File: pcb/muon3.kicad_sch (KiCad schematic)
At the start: 0 parts

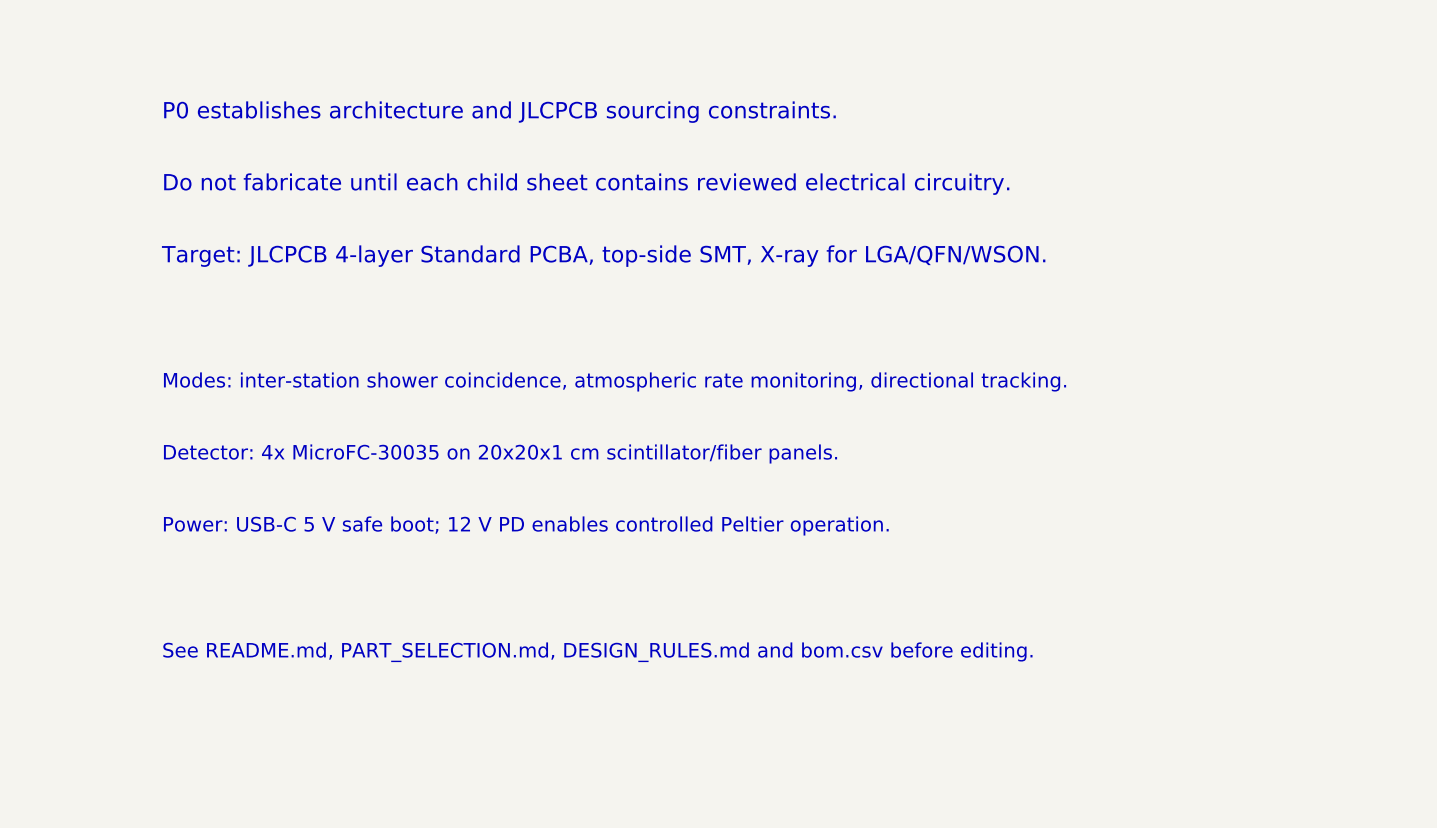
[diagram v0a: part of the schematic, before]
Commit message: Update paper with latest architecture, add openEMS EM simulations (RF, SI, PDN), update schematics with real symbols/wires, add 3D models and openEMS figures
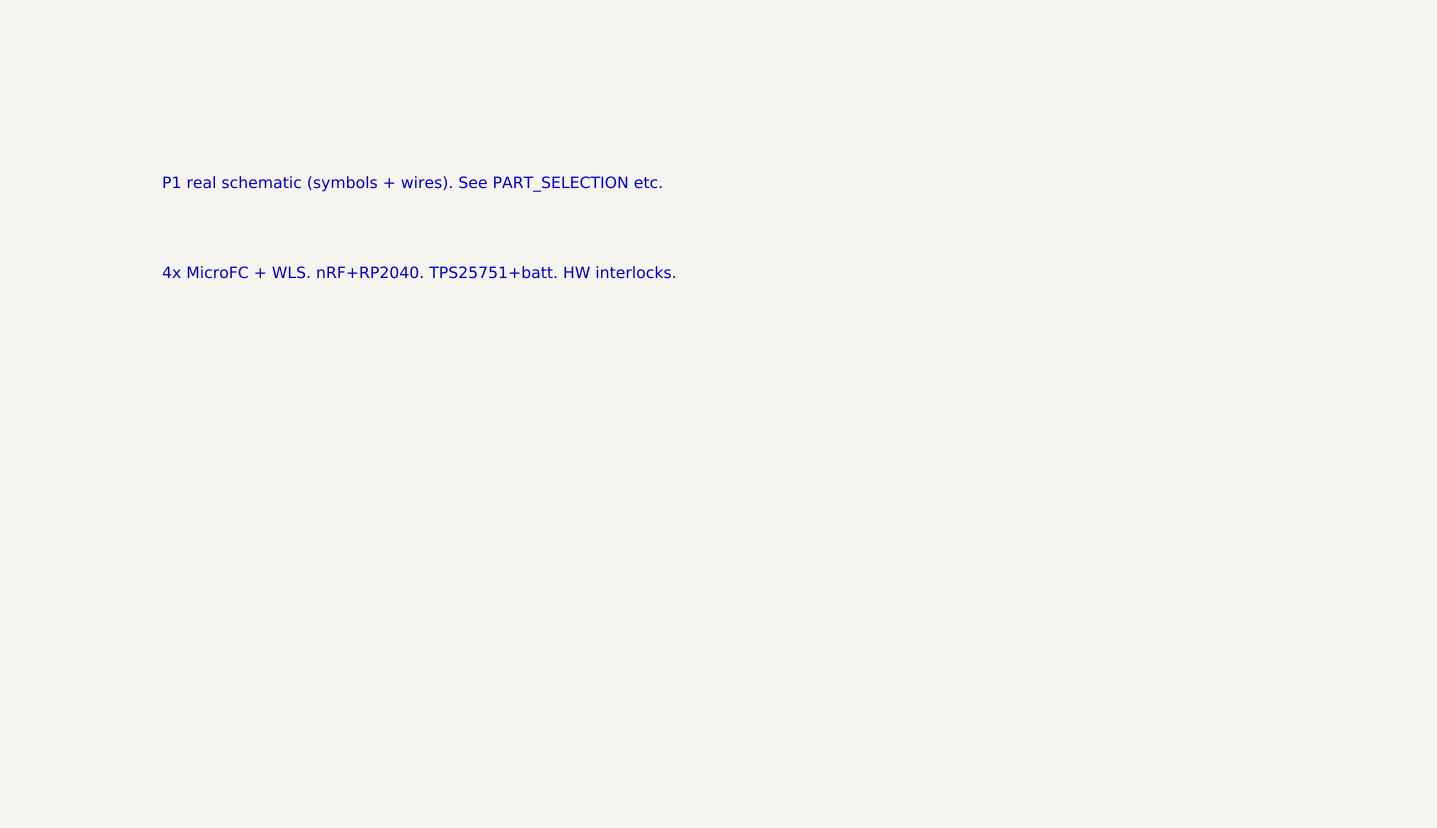
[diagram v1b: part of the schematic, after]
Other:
- note added: "4x MicroFC + WLS. nRF+RP2040. TPS25751+batt. HW interlocks."
- note added: "P1 real schematic (symbols + wires). See PART_SELECTION etc."
- note removed: "Detector: 4x MicroFC-30035 on 20x20x1 cm scintillator/fiber panels."
- note removed: "Do not fabricate until each child sheet contains reviewed electrical circuitry."
- note removed: "Modes: inter-station shower coincidence, atmospheric rate monitoring, directional tracking."
- note removed: "P0 establishes architecture and JLCPCB sourcing constraints."
- note removed: "Power: USB-C 5 V safe boot; 12 V PD enables controlled Peltier operation."
- note removed: "See README.md, PART_SELECTION.md, DESIGN_RULES.md and bom.csv before editing."
- note removed: "Target: JLCPCB 4-layer Standard PCBA, top-side SMT, X-ray for LGA/QFN/WSON."
